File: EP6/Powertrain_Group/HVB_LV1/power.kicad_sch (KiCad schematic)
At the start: 18 parts, among them U10 TPS5430DDA

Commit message: Inverter board adjust
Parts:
- L1: footprint SamacSys_Parts:SRR1260A220M -> Inductor_SMD:L_Bourns_SRR1260
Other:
- moved on the sheet: C23, C24, C25, C26, D14, L1, R28, R30

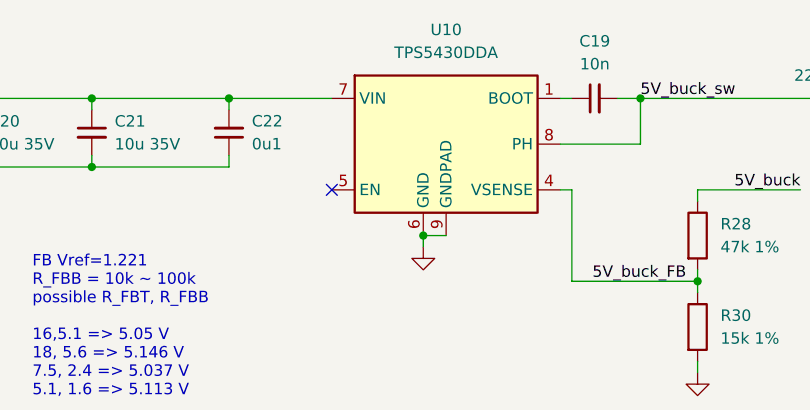
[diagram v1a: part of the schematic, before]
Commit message: update HVB_LV1 to V2.0
split outboard connectors out to a connector board
change led controls to CC control
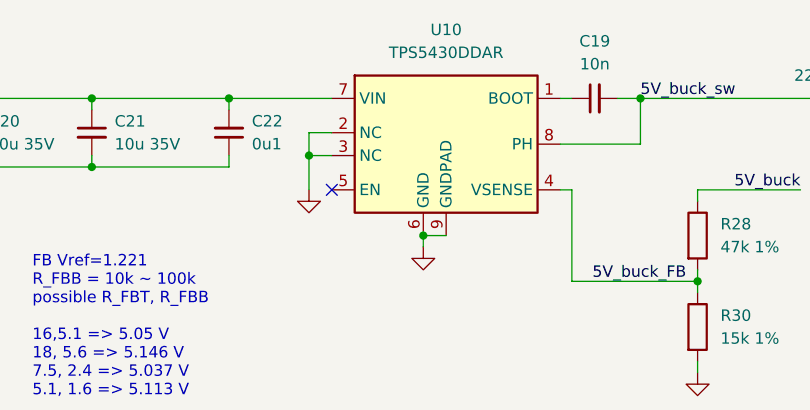
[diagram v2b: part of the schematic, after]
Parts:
- removed U10: TPS5430DDA, Package_SO:TI_SO-PowerPAD-8_ThermalVias, symbol Regulator_Switching:TPS5430DDA
- added U10: TPS5430DDAR, Package_SO:TI_SO-PowerPAD-8_ThermalVias, symbol nturt_kicad_lib_EP6:TPS5430DDAR
- D13: footprint Diode_SMD:D_SMB -> Diode_SMD:D_SOD-123
- F1: footprint Fuse:Fuse_1812_4532Metric -> Fuse:Fuse_1206_3216Metric
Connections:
- net 5V_buck_FB: now also U10.4 (VSENSE)
- net 5V_buck_sw: now also U10.8 (PH)
- net GND: now also U10.2 (NC), U10.3 (NC), U10.6 (GND), U10.9 (GNDPAD)
- net VBUS: now also U10.7 (VIN)
- net at C19.1: now also U10.1 (BOOT)
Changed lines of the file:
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@@
 	(title_block
 		(title "HVB_LV1")
-		(date "2024-10-25")
-		(rev "1.0")
+		(date "2024-12-01")
+		(rev "2.0")
 		(company "NTURacing")
 		(comment 1 "Powertrain")
 		(comment 2 "郭哲明 Jack Kuo")
+	)
+	(junction
+		(at 78.74 35.56)
+		(diameter 0)
+		(color 0 0 0 0)
 	)
 	(junction
@@
 	)
 	(junction
+		(at 91.44 44.45)
+		(diameter 0)
+		(color 0 0 0 0)
+	)
+	(junction
 		(at 139.7 29.21)
 		(diameter 0)
@@
 	)
 	(junction
-		(at 91.44 44.45)
-		(diameter 0)
-		(color 0 0 0 0)
-	)
-	(junction
 		(at 170.18 29.21)
 		(diameter 0)
@@
 	(wire
 		(pts
+			(xy 78.74 33.02) (xy 78.74 35.56)
+		)
+		(stroke
+			(width 0)
+			(type default)
+		)
+	)
+	(wire
+		(pts
 			(xy 182.88 29.21) (xy 195.58 29.21)
 		)
@@
 	(wire
 		(pts
+			(xy 78.74 35.56) (xy 81.28 35.56)
+		)
+		(stroke
+			(width 0)
+			(type default)
+		)
+	)
+	(wire
+		(pts
 			(xy 213.36 29.21) (xy 213.36 30.48)
 		)
@@
 	(wire
 		(pts
+			(xy 78.74 39.37) (xy 78.74 35.56)
+		)
+		(stroke
+			(width 0)
+			(type default)
+		)
+	)
+	(wire
+		(pts
 			(xy 139.7 39.37) (xy 139.7 38.1)
 		)
@@
 		(pts
 			(xy 182.88 36.83) (xy 182.88 35.56)
+		)
+		(stroke
+			(width 0)
+			(type default)
+		)
+	)
+	(wire
+		(pts
+			(xy 81.28 33.02) (xy 78.74 33.02)
 		)
 		(stroke
@@
 	)
 	(symbol
+		(lib_id "nturt_kicad_lib_EP6:TPS5430DDAR")
+		(at 93.98 34.29 0)
+		(unit 1)
+		(exclude_from_sim no)
+		(in_bom yes)
+		(on_board yes)
+		(dnp no)
+		(fields_autoplaced yes)
+		(property "Reference" "U10"
+			(at 93.98 21.59 0)
+			(effects
+				(font
+					(size 1.27 1.27)
+				)
+			)
+		)
+		(property "Value" "TPS5430DDAR"
+			(at 93.98 24.13 0)
+			(effects
+				(font
+					(size 1.27 1.27)
+				)
+			)
+		)
+		(property "Footprint" "Package_SO:TI_SO-PowerPAD-8_ThermalVias"
+			(at 95.25 43.18 0)
+			(effects
+				(font
+					(size 1.27 1.27)
+					(italic yes)
+				)
+				(justify left)
+				(hide yes)
+			)
+		)
+		(property "Datasheet" "http://www.ti.com/lit/ds/symlink/tps5430.pdf"
+			(at 93.98 34.29 0)
+			(effects
+				(font
+					(size 1.27 1.27)
+				)
+				(hide yes)
+			)
+		)
+		(property "Description" "3A, Step Down Swift Converter, Adjustable Output Voltage, 5.5-36V Input Voltage, PowerSO-8"
+			(at 93.98 34.29 0)
+			(effects
+				(font
+					(size 1.27 1.27)
+				)
+				(hide yes)
+			)
+		)
+		(pin "2"
+		)
+		(pin "3"
+		)
+		(pin "5"
+		)
+		(pin "8"
+		)
+		(pin "9"
+		)
+		(pin "6"
+		)
+		(pin "4"
+		)
+		(pin "1"
+		)
+		(pin "7"
+		)
+		(instances
+			(project "HVB_LV1"
+				(path "/e268df90-efd0-451f-9c39-af40eeef0439/8ccb6400-0ecc-48e8-87c6-ba8bc9bb1e9c"
+					(reference "U10")
+					(unit 1)
+				)
+			)
+		)
+	)
+	(symbol
 		(lib_id "Connector:TestPoint")
 		(at 213.36 27.94 0)
@@
 	)
 	(symbol
+		(lib_id "power:GND")
+		(at 78.74 39.37 0)
+		(unit 1)
+		(exclude_from_sim no)
+		(in_bom yes)
+		(on_board yes)
+		(dnp no)
+		(fields_autoplaced yes)
+		(property "Reference" "#PWR03"
+			(at 78.74 45.72 0)
+			(effects
+				(font
+					(size 1.27 1.27)
+				)
+				(hide yes)
+			)
+		)
+		(property "Value" "GND"
+			(at 78.74 44.45 0)
+			(effects
+				(font
+					(size 1.27 1.27)
+				)
+				(hide yes)
+			)
+		)
+		(property "Footprint" ""
+			(at 78.74 39.37 0)
+			(effects
+				(font
+					(size 1.27 1.27)
+				)
+				(hide yes)
+			)
+		)
+		(property "Datasheet" ""
+			(at 78.74 39.37 0)
+			(effects
+				(font
+					(size 1.27 1.27)
+				)
+				(hide yes)
+			)
+		)
+		(property "Description" "Power symbol creates a global label with name \"GND\" , ground"
+			(at 78.74 39.37 0)
+			(effects
+				(font
+					(size 1.27 1.27)
+				)
+				(hide yes)
+			)
+		)
+		(pin "1"
+		)
+		(instances
+			(project "HVB_LV1"
+				(path "/e268df90-efd0-451f-9c39-af40eeef0439/8ccb6400-0ecc-48e8-87c6-ba8bc9bb1e9c"
+					(reference "#PWR03")
+					(unit 1)
+				)
+			)
+		)
+	)
+	(symbol
 		(lib_id "Device:C_Small")
 		(at 170.18 33.02 0)
@@
 			)
 		)
-		(property "Footprint" "Fuse:Fuse_1812_4532Metric"
+		(property "Footprint" "Fuse:Fuse_1206_3216Metric"
 			(at 203.2 29.21 0)
 			(effects
@@
 	)
 	(symbol
-		(lib_id "Regulator_Switching:TPS5430DDA")
-		(at 93.98 34.29 0)
-		(unit 1)
-		(exclude_from_sim no)
-		(in_bom yes)
-		(on_board yes)
-		(dnp no)
-		(fields_autoplaced yes)
-		(property "Reference" "U10"
-			(at 93.98 21.59 0)
-			(effects
-				(font
-					(size 1.27 1.27)
-				)
-			)
-		)
-		(property "Value" "TPS5430DDA"
-			(at 93.98 24.13 0)
-			(effects
-				(font
-					(size 1.27 1.27)
-				)
-			)
-		)
-		(property "Footprint" "Package_SO:TI_SO-PowerPAD-8_ThermalVias"
-			(at 95.25 43.18 0)
-			(effects
-				(font
-					(size 1.27 1.27)
-					(italic yes)
-				)
-				(justify left)
-				(hide yes)
-			)
-		)
-		(property "Datasheet" "http://www.ti.com/lit/ds/symlink/tps5430.pdf"
-			(at 93.98 34.29 0)
-			(effects
-				(font
-					(size 1.27 1.27)
-				)
-				(hide yes)
-			)
-		)
-		(property "Description" "3A, Step Down Swift Converter, Adjustable Output Voltage, 5.5-36V Input Voltage, PowerSO-8"
-			(at 93.98 34.29 0)
-			(effects
-				(font
-					(size 1.27 1.27)
-				)
-				(hide yes)
-			)
-		)
-		(pin "2"
-		)
-		(pin "3"
-		)
-		(pin "5"
-		)
-		(pin "8"
-		)
-		(pin "9"
-		)
-		(pin "6"
-		)
-		(pin "4"
-		)
-		(pin "1"
-		)
-		(pin "7"
-		)
-		(instances
-			(project "HVB_LV1"
-				(path "/e268df90-efd0-451f-9c39-af40eeef0439/8ccb6400-0ecc-48e8-87c6-ba8bc9bb1e9c"
-					(reference "U10")
-					(unit 1)
-				)
-			)
-		)
-	)
-	(symbol
 		(lib_id "Device:R")
 		(at 213.36 44.45 0)
@@
 			)
 		)
-		(property "Footprint" "Diode_SMD:D_SMB"
+		(property "Footprint" "Diode_SMD:D_SOD-123"
 			(at 227.33 39.37 90)
 			(effects

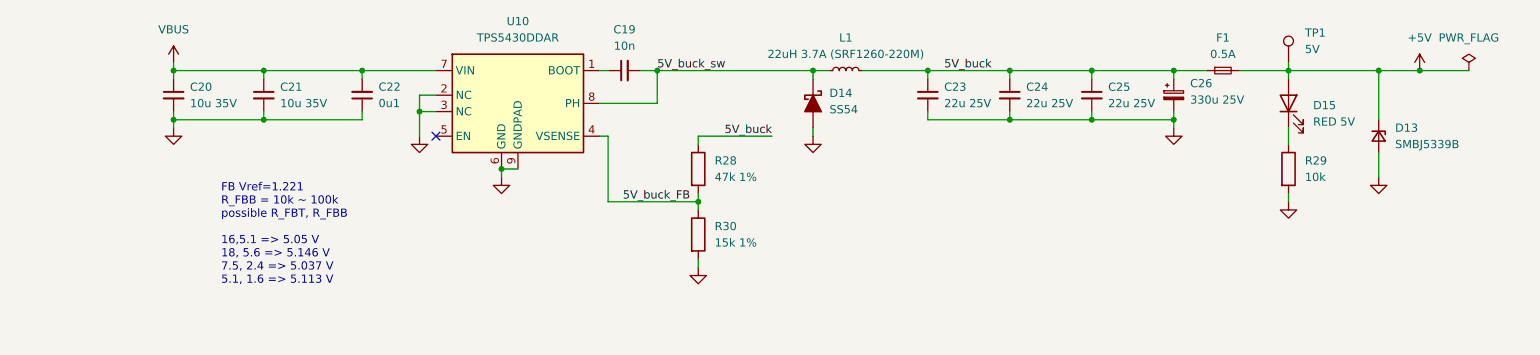
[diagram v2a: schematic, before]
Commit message: update HVB_LV1 to V2.0
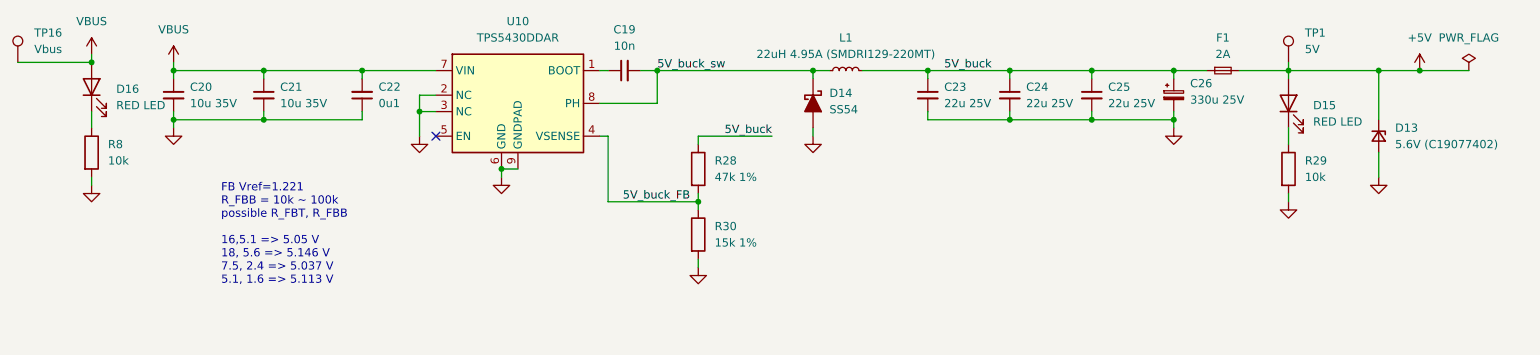
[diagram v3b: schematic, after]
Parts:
- added D16: RED LED, LED_SMD:LED_0603_1608Metric, symbol Device:LED
- added R8: 10k, Resistor_SMD:R_0603_1608Metric, symbol Device:R
- added TP16: Vbus, TestPoint:TestPoint_Pad_D1.0mm, symbol Connector:TestPoint
- D13: value SMBJ5339B -> 5.6V (C19077402)
- D15: value RED 5V -> RED LED
- F1: value 0.5A -> 2A
- L1: value 22uH 3.7A (SRF1260-220M) -> 22uH 4.95A (SMDRI129-220MT)
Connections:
- net GND: now also R8.2
- net VBUS: now also D16.2 (A), TP16.1
- new net: D16.1 (K), R8.1

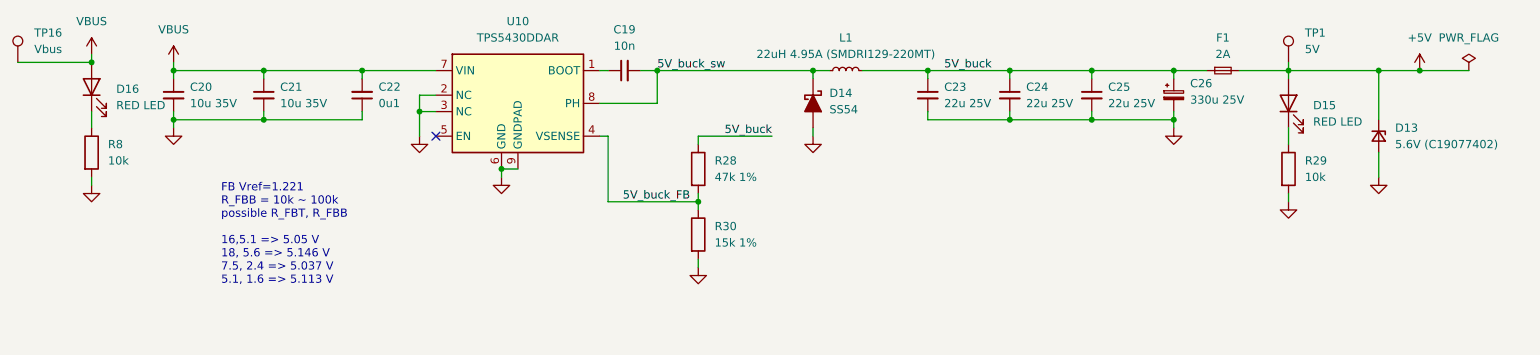
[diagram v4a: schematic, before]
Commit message: update HVB_LV1 to V3.0
fix many problems from V2.2
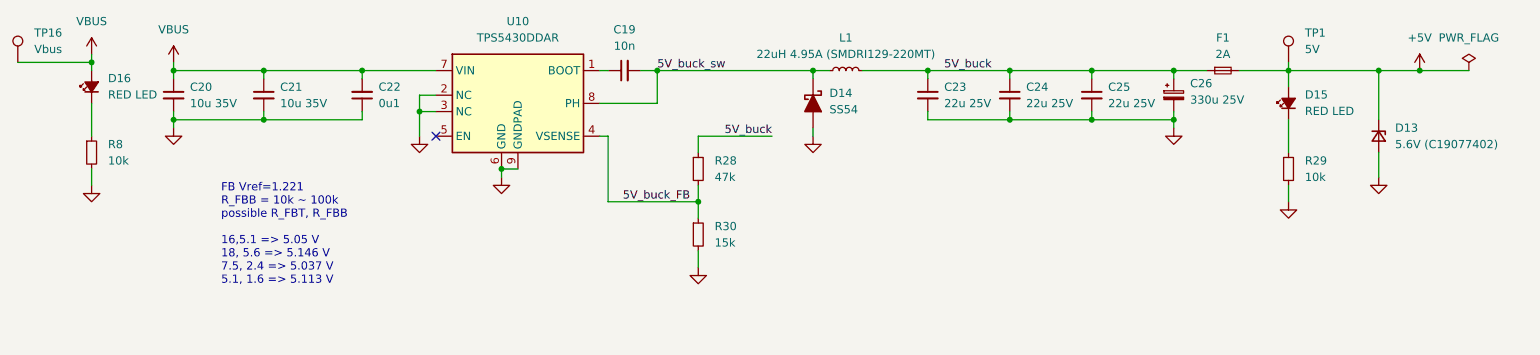
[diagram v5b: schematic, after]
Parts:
- D15, D16: symbol Device:LED -> Device:LED_Small_Filled
- R28: value 47k 1% -> 47k; symbol Device:R -> Device:R_Small
- R29, R8: symbol Device:R -> Device:R_Small
- R30: value 15k 1% -> 15k; symbol Device:R -> Device:R_Small
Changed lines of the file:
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@@
 	(title_block
 		(title "HVB_LV1")
-		(date "2024-12-05")
-		(rev "2.2")
+		(date "2025-03-19")
+		(rev "3.0")
 		(company "NTURacing")
 		(comment 1 "Powertrain")
@@
 	)
 	(junction
-		(at 27.94 27.94)
+		(at 69.85 29.21)
 		(diameter 0)
 		(color 0 0 0 0)
 	)
 	(junction
-		(at 69.85 29.21)
+		(at 27.94 27.94)
 		(diameter 0)
 		(color 0 0 0 0)
@@
 	(wire
 		(pts
-			(xy 121.92 59.69) (xy 121.92 58.42)
-		)
-		(stroke
-			(width 0)
-			(type default)
-		)
-	)
-	(wire
-		(pts
-			(xy 121.92 39.37) (xy 121.92 40.64)
-		)
-		(stroke
-			(width 0)
-			(type default)
-		)
-	)
-	(wire
-		(pts
 			(xy 157.48 36.83) (xy 170.18 36.83)
 		)
@@
 	(wire
 		(pts
+			(xy 213.36 46.99) (xy 213.36 49.53)
+		)
+		(stroke
+			(width 0)
+			(type default)
+		)
+	)
+	(wire
+		(pts
 			(xy 170.18 36.83) (xy 170.18 35.56)
 		)
@@
 	(wire
 		(pts
-			(xy 121.92 49.53) (xy 121.92 50.8)
+			(xy 121.92 49.53) (xy 121.92 52.07)
 		)
 		(stroke
@@
 	(wire
 		(pts
-			(xy 213.36 49.53) (xy 213.36 48.26)
-		)
-		(stroke
-			(width 0)
-			(type default)
-		)
-	)
-	(wire
-		(pts
 			(xy 40.64 29.21) (xy 54.61 29.21)
 		)
@@
 	(wire
 		(pts
-			(xy 213.36 29.21) (xy 213.36 30.48)
-		)
-		(stroke
-			(width 0)
-			(type default)
-		)
-	)
-	(wire
-		(pts
 			(xy 139.7 30.48) (xy 139.7 29.21)
 		)
@@
 	(wire
 		(pts
-			(xy 27.94 38.1) (xy 27.94 35.56)
+			(xy 27.94 34.29) (xy 27.94 39.37)
 		)
 		(stroke
@@
 	(wire
 		(pts
-			(xy 213.36 40.64) (xy 213.36 38.1)
+			(xy 213.36 29.21) (xy 213.36 31.75)
 		)
 		(stroke
@@
 	(wire
 		(pts
+			(xy 121.92 57.15) (xy 121.92 59.69)
+		)
+		(stroke
+			(width 0)
+			(type default)
+		)
+	)
+	(wire
+		(pts
 			(xy 157.48 30.48) (xy 157.48 29.21)
 		)
@@
 	(wire
 		(pts
+			(xy 213.36 36.83) (xy 213.36 41.91)
+		)
+		(stroke
+			(width 0)
+			(type default)
+		)
+	)
+	(wire
+		(pts
 			(xy 182.88 36.83) (xy 182.88 35.56)
 		)
@@
 	(wire
 		(pts
+			(xy 27.94 44.45) (xy 27.94 46.99)
+		)
+		(stroke
+			(width 0)
+			(type default)
+		)
+	)
+	(wire
+		(pts
 			(xy 195.58 29.21) (xy 200.66 29.21)
 		)
@@
 	(wire
 		(pts
-			(xy 27.94 46.99) (xy 27.94 45.72)
+			(xy 27.94 27.94) (xy 27.94 29.21)
 		)
 		(stroke
@@
 	(wire
 		(pts
+			(xy 121.92 46.99) (xy 121.92 49.53)
+		)
+		(stroke
+			(width 0)
+			(type default)
+		)
+	)
+	(wire
+		(pts
 			(xy 133.35 39.37) (xy 121.92 39.37)
 		)
@@
 	(wire
 		(pts
-			(xy 121.92 48.26) (xy 121.92 49.53)
+			(xy 121.92 39.37) (xy 121.92 41.91)
 		)
 		(stroke
@@
 	(label "5V_buck"
 		(at 133.35 39.37 180)
-		(fields_autoplaced yes)
 		(effects
 			(font
@@
 	(label "5V_buck_FB"
 		(at 120.65 49.53 180)
-		(fields_autoplaced yes)
 		(effects
 			(font
@@
 	(label "5V_buck"
 		(at 160.02 29.21 0)
-		(fields_autoplaced yes)
 		(effects
 			(font
@@
 	(label "5V_buck_sw"
 		(at 115.57 29.21 0)
-		(fields_autoplaced yes)
 		(effects
 			(font
@@
 	)
 	(symbol
-		(lib_id "Device:R")
+		(lib_id "Device:R_Small")
 		(at 121.92 54.61 0)
 		(unit 1)
@@
 			)
 		)
-		(property "Value" "15k 1%"
+		(property "Value" "15k"
 			(at 124.46 55.88 0)
 			(effects
@@
 		)
 		(property "Footprint" "Resistor_SMD:R_0603_1608Metric"
-			(at 120.142 54.61 90)
+			(at 121.92 54.61 0)
 			(effects
 				(font
@@
 			)
 		)
-		(property "Description" "Resistor"
+		(property "Description" "Resistor, small symbol"
 			(at 121.92 54.61 0)
 			(effects
@@
 	)
 	(symbol
-		(lib_id "Device:R")
+		(lib_id "Device:R_Small")
 		(at 121.92 44.45 0)
 		(unit 1)
@@
 			)
 		)
-		(property "Value" "47k 1%"
+		(property "Value" "47k"
 			(at 124.46 45.72 0)
 			(effects
@@
 		)
 		(property "Footprint" "Resistor_SMD:R_0603_1608Metric"
-			(at 120.142 44.45 90)
+			(at 121.92 44.45 0)
 			(effects
 				(font
@@
 			)
 		)
-		(property "Description" "Resistor"
+		(property "Description" "Resistor, small symbol"
 			(at 121.92 44.45 0)
 			(effects
@@
 	)
 	(symbol
-		(lib_id "Device:LED")
+		(lib_id "Device:LED_Small_Filled")
 		(at 27.94 31.75 90)
 		(unit 1)
@@
 		(fields_autoplaced yes)
 		(property "Reference" "D16"
-			(at 31.75 32.0675 90)
+			(at 30.48 30.4165 90)
 			(effects
 				(font
@@
 		)
 		(property "Value" "RED LED"
-			(at 31.75 34.6075 90)
+			(at 30.48 32.9565 90)
 			(effects
 				(font
@@
 		)
 		(property "Footprint" "LED_SMD:LED_0603_1608Metric"
-			(at 27.94 31.75 0)
+			(at 27.94 31.75 90)
 			(effects
 				(font
@@
 		)
 		(property "Datasheet" "~"
-			(at 27.94 31.75 0)
-			(effects
-				(font
-					(size 1.27 1.27)
-				)
-				(hide yes)
-			)
-		)
-		(property "Description" "Light emitting diode"
+			(at 27.94 31.75 90)
+			(effects
+				(font
+					(size 1.27 1.27)
+				)
+				(hide yes)
+			)
+		)
+		(property "Description" "Light emitting diode, small symbol, filled shape"
 			(at 27.94 31.75 0)
 			(effects
@@
 	)
 	(symbol
-		(lib_id "Device:R")
+		(lib_id "Device:R_Small")
 		(at 213.36 44.45 0)
 		(unit 1)
@@
 		)
 		(property "Footprint" "Resistor_SMD:R_0603_1608Metric"
-			(at 211.582 44.45 90)
+			(at 213.36 44.45 0)
 			(effects
 				(font
@@
 			)
 		)
-		(property "Description" "Resistor"
+		(property "Description" "Resistor, small symbol"
 			(at 213.36 44.45 0)
 			(effects
@@
 	)
 	(symbol
-		(lib_id "Device:LED")
+		(lib_id "Device:LED_Small_Filled")
 		(at 213.36 34.29 90)
 		(unit 1)
@@
 		(fields_autoplaced yes)
 		(property "Reference" "D15"
-			(at 217.17 34.6075 90)
+			(at 215.9 32.9565 90)
 			(effects
 				(font
@@
 		)
 		(property "Value" "RED LED"
-			(at 217.17 37.1475 90)
+			(at 215.9 35.4965 90)
 			(effects
 				(font
@@
 		)
 		(property "Footprint" "LED_SMD:LED_0603_1608Metric"
-			(at 213.36 34.29 0)
+			(at 213.36 34.29 90)
 			(effects
 				(font
@@
 		)
 		(property "Datasheet" "~"
-			(at 213.36 34.29 0)
-			(effects
-				(font
-					(size 1.27 1.27)
-				)
-				(hide yes)
-			)
-		)
-		(property "Description" "Light emitting diode"
+			(at 213.36 34.29 90)
+			(effects
+				(font
+					(size 1.27 1.27)
+				)
+				(hide yes)
+			)
+		)
+		(property "Description" "Light emitting diode, small symbol, filled shape"
 			(at 213.36 34.29 0)
 			(effects
@@
 	)
 	(symbol
-		(lib_id "Device:R")
+		(lib_id "Device:R_Small")
 		(at 27.94 41.91 0)
 		(unit 1)
@@
 		)
 		(property "Footprint" "Resistor_SMD:R_0603_1608Metric"
-			(at 26.162 41.91 90)
+			(at 27.94 41.91 0)
 			(effects
 				(font
@@
 			)
 		)
-		(property "Description" "Resistor"
+		(property "Description" "Resistor, small symbol"
 			(at 27.94 41.91 0)
 			(effects
